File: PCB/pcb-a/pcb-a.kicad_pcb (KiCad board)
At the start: 2 copper layers, 94.9 x 43.5 mm, 43 parts, among them J1 Conn_02x05_Counter_Clockwise, J2 Conn_02x05_Counter_Clockwise, Q1 BC807, Q2 BC807, Q3 BC817, Q4 BC807, Q5 BC807, Q6 BC807, SW1 config, U1 ESP32-S2-DevKitM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

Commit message: Many changes and fixes
Electric schema A & B
	- Wrong (undefined) signals direction fixed
	- More readable schema getting: c_<signal> color has changed
	- Some pull-up resistors has been added for safing purpose
	- Wire connectors holes size reducing
	- Because Led indicatord uses less then 500mA, their wire connectors have been substituted by pin-header ones

PCB
	- Updates for schema changes
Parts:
- added R21: 100K, Resistor_SMD:R_1206_3216Metric, B.Cu at (178.6, 67.1)
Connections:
- net 5V renamed +5V
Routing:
- net o_startEngine: track 44.6 -> 52.1 mm, vias 2 -> 3
- net GND: track 218.7 -> 221.2 mm, vias 5 -> 6
- net +5V: track 286.2 -> 288.0 mm, vias 10 -> 11

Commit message: Some warning message has been fixed
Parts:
- moved R12 2.05 mm to (159.6, 98.8)
- moved Q2 1.62 mm to (162.8, 100.0)
- moved Q5 1.50 mm to (166.4, 99.4)
- moved R13 0.92 mm to (160.7, 103.0)
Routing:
- net +5V: track 288.0 -> 269.5 mm, vias 11 -> 9
- net c_rightArrow: track 16.7 -> 14.7 mm
- net Net-(Q2-B): track 7.09 -> 8.78 mm
- net Net-(Q5-B): track 1.21 -> 2.53 mm
- net c_brakeSwitch: track 11.6 -> 10.4 mm
- net GND: track 221.2 -> 222.0 mm
- net Net-(Q5-C): track 6.24 -> 5.47 mm
- net Net-(Q2-C): track 2.24 -> 2.91 mm

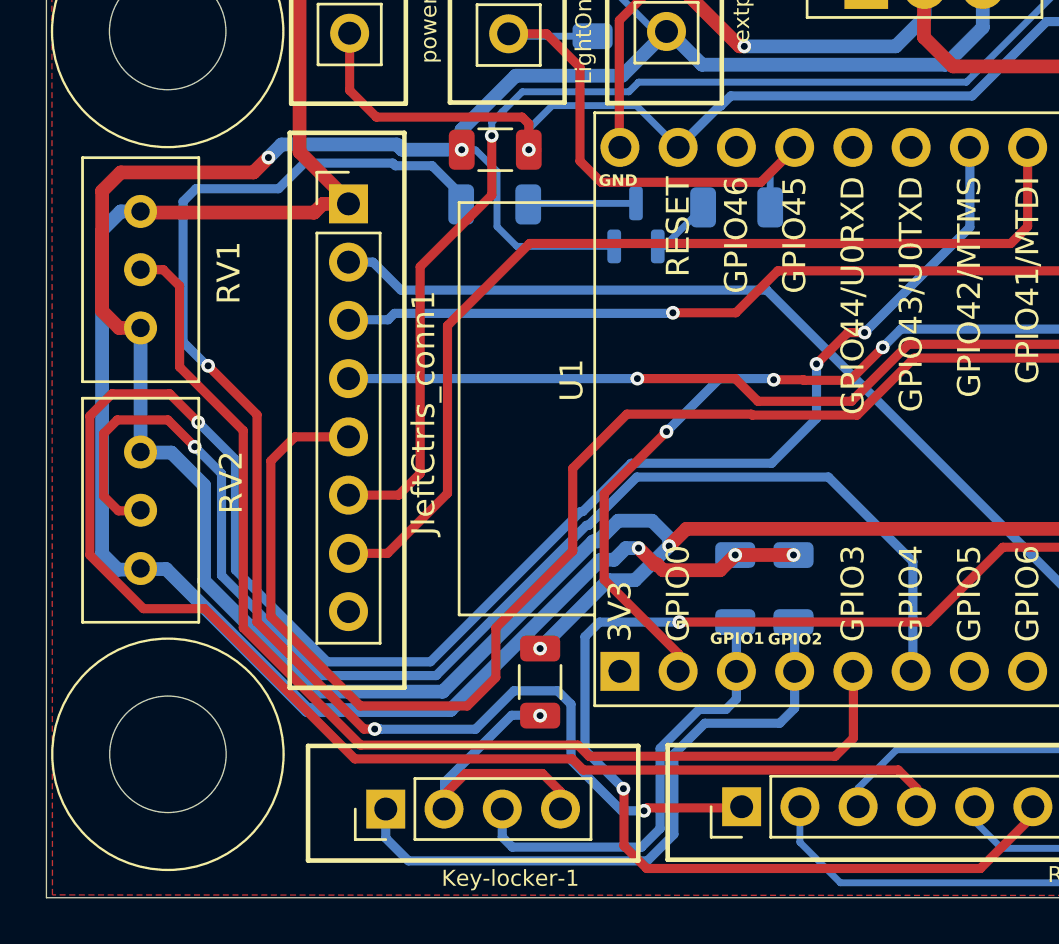
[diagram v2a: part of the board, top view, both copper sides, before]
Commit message: Merging from main
Key authentication physical references removed
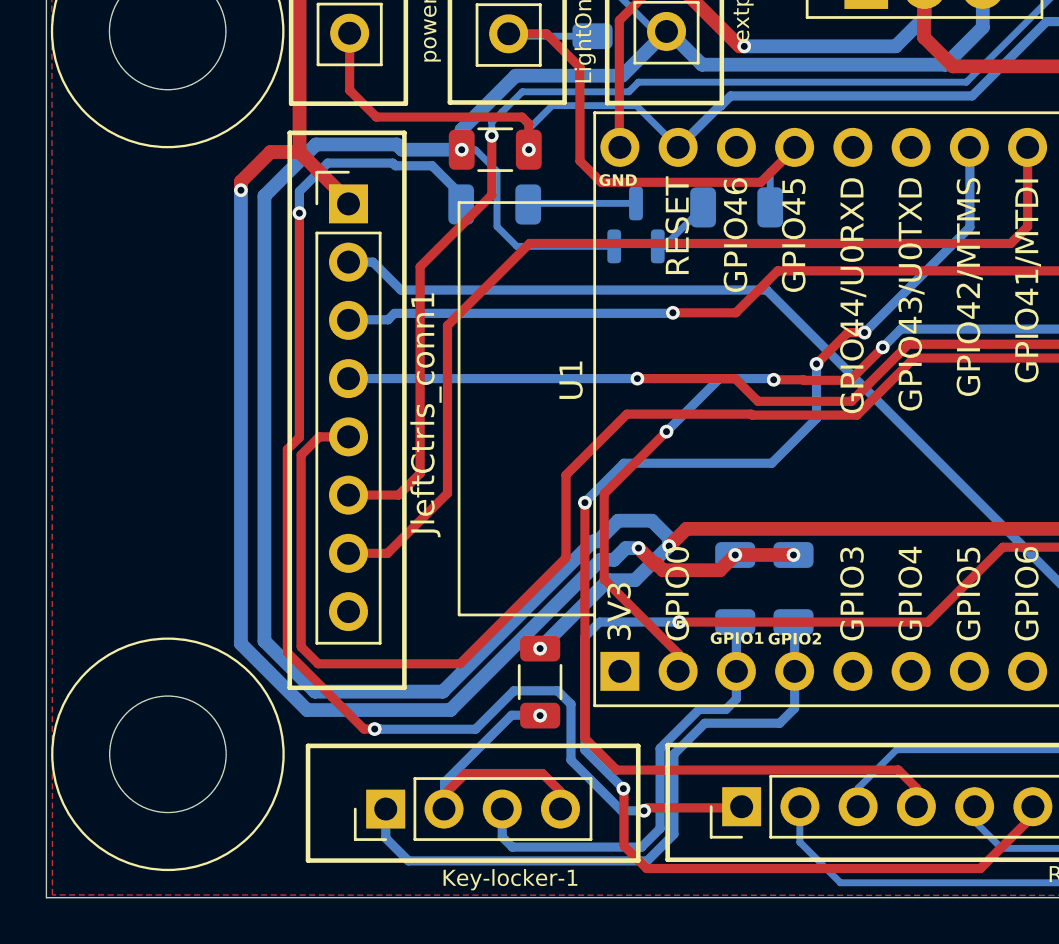
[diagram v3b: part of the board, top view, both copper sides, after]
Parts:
- removed RV1, RV2: 10K, Potentiometer_THT:Potentiometer_Bourns_3296W_Vertical
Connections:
- U1 pad 5: Net-(U1-GPIO3/TOUCH3/ADC1_CH2) -> unconnected-(U1-GPIO3/TOUCH3/ADC1_CH2-Pad5)
- U1 pad 6: Net-(U1-GPIO4/TOUCH4/ADC1_CH3) -> unconnected-(U1-GPIO4/TOUCH4/ADC1_CH3-Pad6)
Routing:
- net Net-(U1-GPIO4/TOUCH4/ADC1_CH3): track 57.3 -> 0.00 mm, vias 1 -> 0
- net i_bykeStand: track 106.4 -> 53.2 mm
- net Net-(U1-GPIO3/TOUCH3/ADC1_CH2): track 50.7 -> 0.00 mm
- net +5V: track 269.5 -> 258.0 mm, vias 9 -> 8
- net GND: track 222.0 -> 212.2 mm, vias 6 -> 7
- net c_rearLight: track 61.0 -> 54.4 mm
- net i_rightArrow: track 83.3 -> 78.8 mm
- net unconnected-(U1-GPIO3/TOUCH3/ADC1_CH2-Pad5): track 0.00 -> 0.52 mm
